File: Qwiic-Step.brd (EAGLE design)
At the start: 44.5 x 44.5 mm, 77 parts, among them J1 PTH, J2 Qwiic Right Angle, J3 POWER_JACKSUPER_BOMB_DIGITY, J4 Qwiic Right Angle, J5 ISP, U1 A49885MM, U2 ATMEGA328P_TQFP, Y1 16MHz

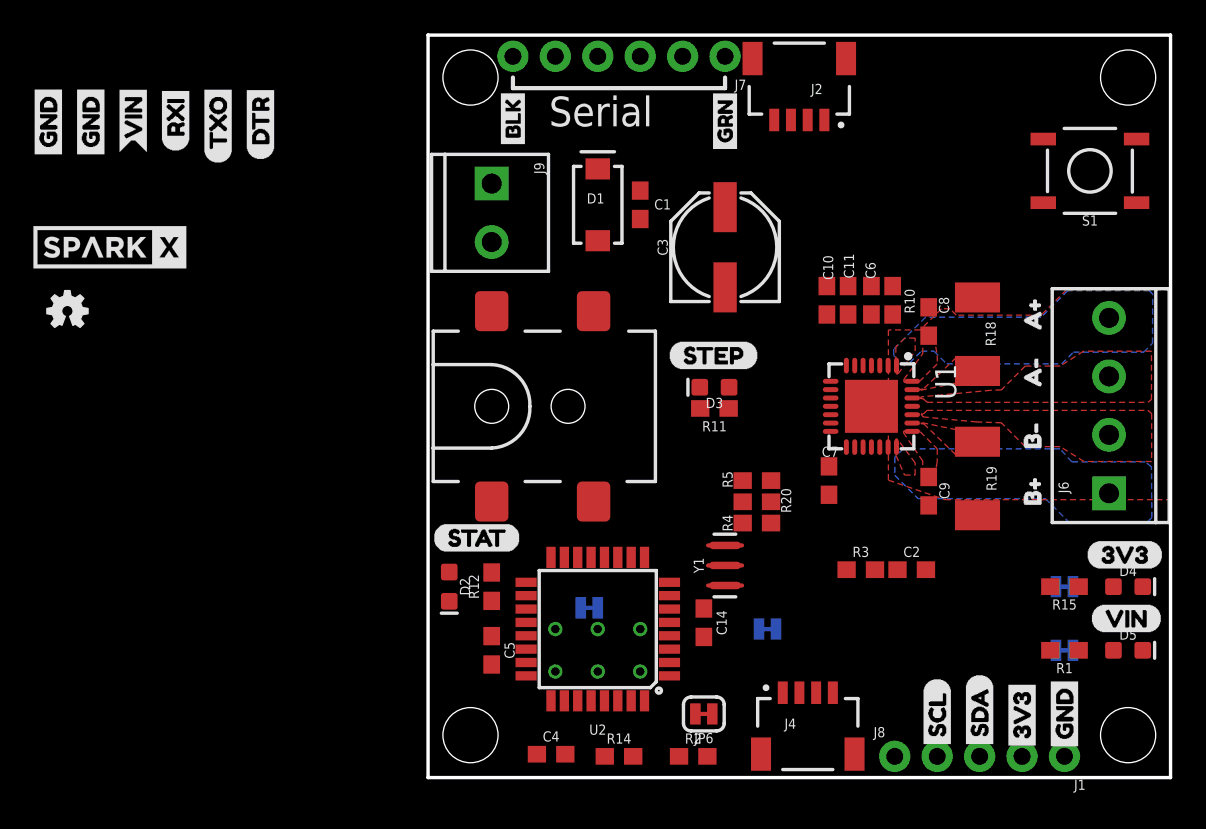
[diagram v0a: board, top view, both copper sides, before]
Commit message: Add limit switches
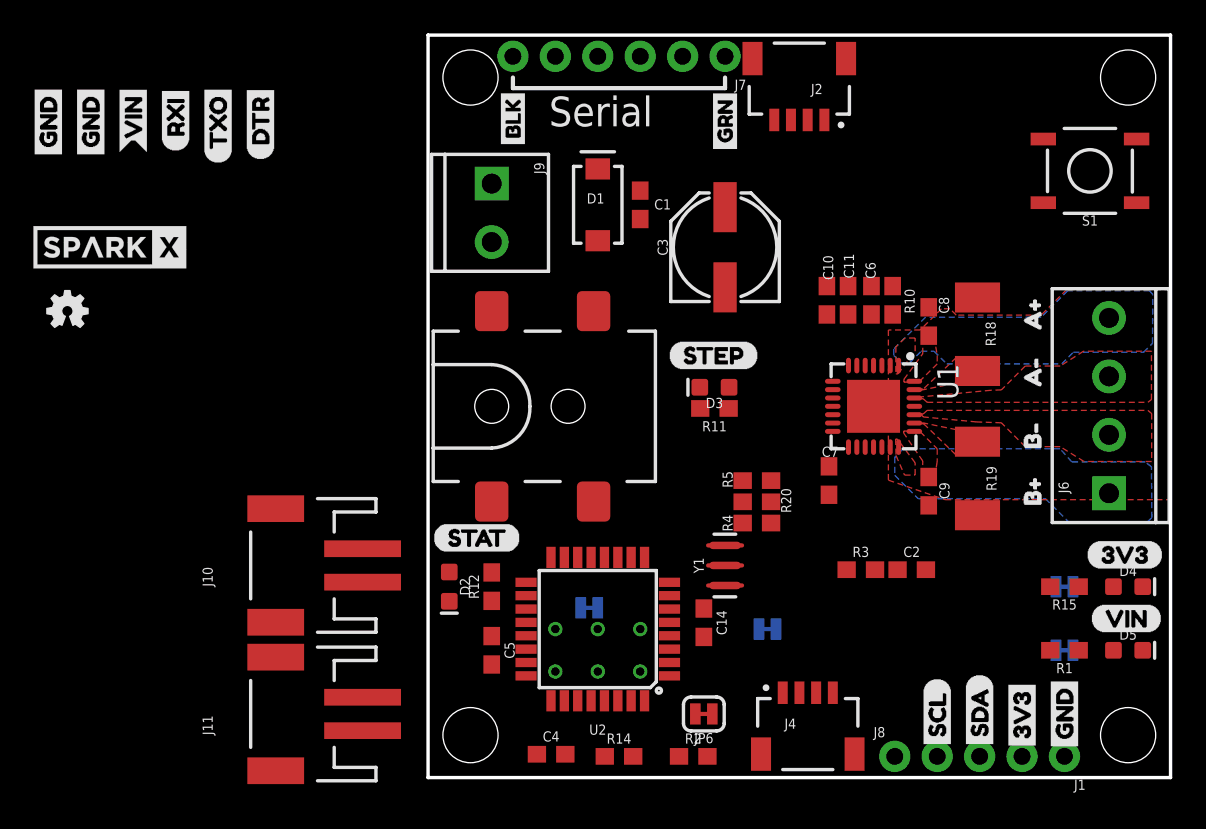
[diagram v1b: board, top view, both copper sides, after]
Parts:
- added J10, J11: (no value), SparkFun-Connectors:JST-2-SMD
- moved U1 0.13 mm to (26.7, 22.2)
